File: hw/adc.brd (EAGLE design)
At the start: 49.6 x 25.6 mm, 42 parts, among them U1 ADS1194CPAG

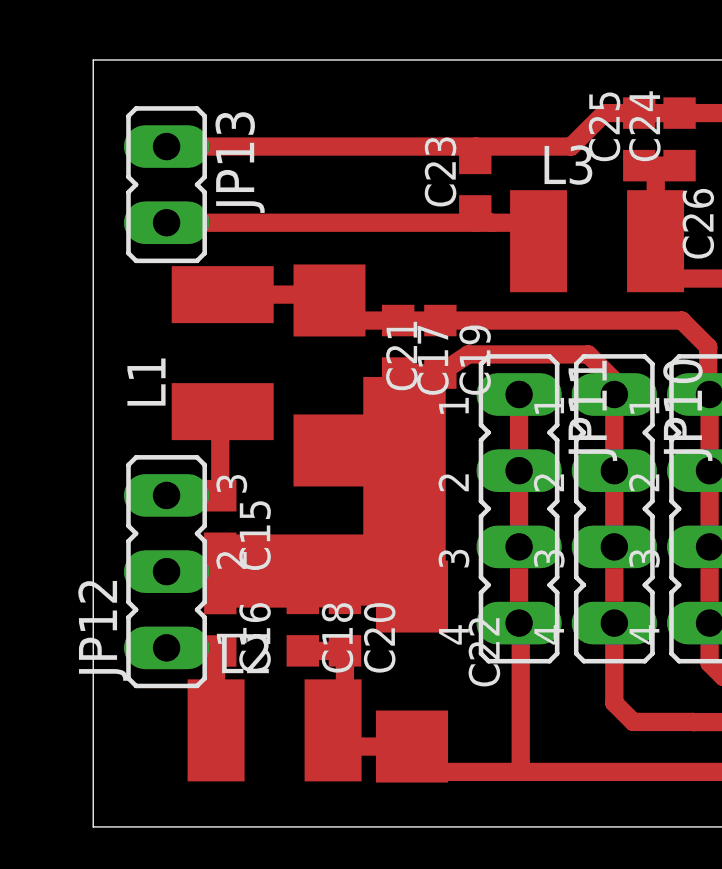
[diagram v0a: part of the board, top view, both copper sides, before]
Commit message: created power board
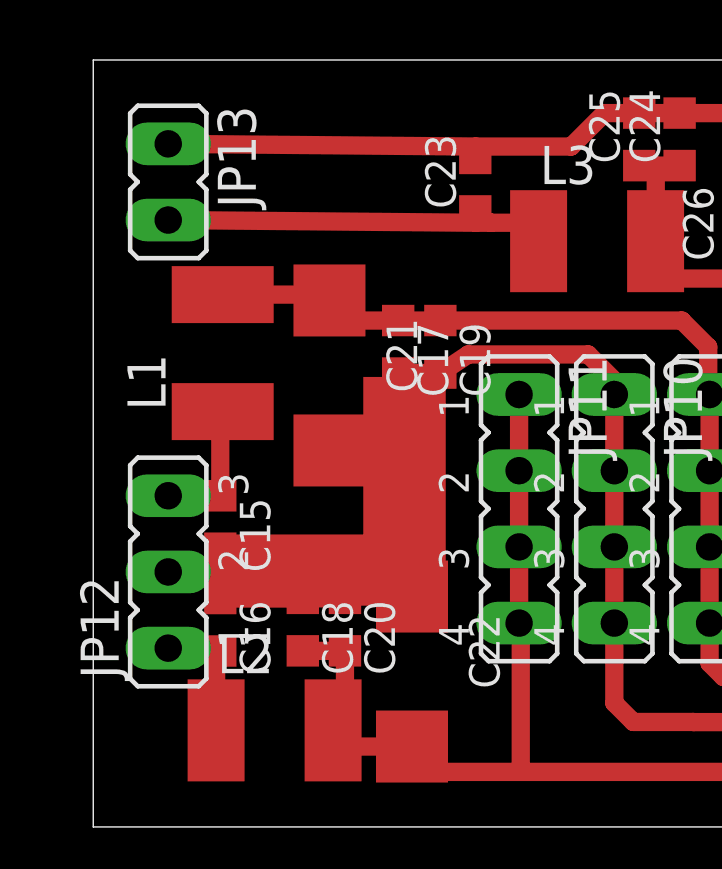
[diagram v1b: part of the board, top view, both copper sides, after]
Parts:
- moved JP13 0.11 mm to (2.50, 21.5)
- moved JP12 0.06 mm to (2.50, 8.50)
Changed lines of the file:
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@@
 <element name="JP10" library="jumper" package="JP4" value="AINgnd" x="17.37" y="10.605" rot="R270"/>
 <element name="JP11" library="jumper" package="JP4" value="AINvss" x="14.195" y="10.605" rot="R270"/>
-<element name="JP12" library="jumper" package="JP2" value="PWR1" x="2.445" y="8.51" rot="R90"/>
-<element name="JP13" library="jumper" package="JP1" value="PWR2" x="2.445" y="21.41" rot="R180"/>
+<element name="JP12" library="jumper" package="JP2" value="PWR1" x="2.5" y="8.5" rot="R90"/>
+<element name="JP13" library="jumper" package="JP1" value="PWR2" x="2.5" y="21.5" rot="R180"/>
 <element name="U1" library="adc-ti" package="QFP50P1200X1200X120-64N" value="ADS1194CPAG" x="36.75" y="12.5">
 <attribute name="PACKAGE" value="TQFP-64" x="36.75" y="12.5" size="1.778" layer="27" display="off"/>
@@
 <contactref element="U1" pad="51"/>
 <contactref element="U1" pad="31"/>
-<wire x1="2.445" y1="22.68" x2="12.75" y2="22.68" width="0.6096" layer="1"/>
+<wire x1="2.5" y1="22.77" x2="12.75" y2="22.68" width="0.6096" layer="1"/>
 <wire x1="12.75" y1="22.68" x2="15.93" y2="22.68" width="0.6096" layer="1"/>
 <wire x1="15.93" y1="22.68" x2="17.045" y2="23.795" width="0.6096" layer="1"/>
@@
 <wire x1="4.315" y1="13.845" x2="4.235" y2="13.845" width="0.6096" layer="1"/>
 <wire x1="4.235" y1="13.845" x2="4.235" y2="11.04" width="0.6096" layer="1"/>
-<wire x1="2.445" y1="11.05" x2="4.235" y2="11.05" width="0.6096" layer="1"/>
+<wire x1="2.5" y1="11.04" x2="4.235" y2="11.05" width="0.6096" layer="1"/>
 <wire x1="4.235" y1="11.05" x2="4.235" y2="11.04" width="0.6096" layer="1"/>
 </signal>
@@
 <contactref element="C16" pad="2"/>
 <contactref element="JP12" pad="1"/>
-<wire x1="2.445" y1="5.97" x2="4.235" y2="5.97" width="0.6096" layer="1"/>
+<wire x1="2.5" y1="5.96" x2="4.235" y2="5.97" width="0.6096" layer="1"/>
 <wire x1="4.235" y1="5.97" x2="4.235" y2="5.865" width="0.6096" layer="1"/>
 <wire x1="4.235" y1="5.865" x2="4.095" y2="5.865" width="0.6096" layer="1"/>
@@
 <contactref element="L3" pad="1"/>
 <contactref element="JP13" pad="2"/>
-<wire x1="2.445" y1="20.14" x2="12.75" y2="20.14" width="0.6096" layer="1"/>
+<wire x1="2.5" y1="20.23" x2="12.75" y2="20.14" width="0.6096" layer="1"/>
 <wire x1="12.75" y1="20.14" x2="13.25" y2="20.14" width="0.6096" layer="1"/>
 <wire x1="13.25" y1="20.14" x2="14.23" y2="20.14" width="0.6096" layer="1"/>
@@
 <wire x1="10" y1="15.13" x2="10" y2="12.55" width="0.6096" layer="1"/>
 <wire x1="10" y1="12.55" x2="10" y2="7.68" width="0.6096" layer="1"/>
-<wire x1="2.445" y1="8.51" x2="4.235" y2="8.51" width="0.6096" layer="1"/>
+<wire x1="2.5" y1="8.5" x2="4.235" y2="8.51" width="0.6096" layer="1"/>
 <wire x1="7.875" y1="12.55" x2="10" y2="12.55" width="0.6096" layer="1"/>
 <wire x1="12.5" y1="15.75" x2="11.57" y2="15.13" width="0.6096" layer="1"/>
